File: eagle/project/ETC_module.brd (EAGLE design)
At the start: 100 x 80 mm, 102 parts, among them IC1 LM358, Q2 MOSFET-PCHANNELFQP27P06, U1 V_REG_317SMD

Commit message: v1.0 of ETC board complete
initial work on GS board underway too
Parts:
- added U$20: (no value), custom:NURLOGO
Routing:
- net GNDI: track 143.3 -> 96.0 mm
- net +5VCLEAN: track 316.0 -> 276.3 mm
- net N$41: track 17.1 -> 18.0 mm
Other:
- board size 100 x 80 mm -> 101.3 x 81.3 mm
- board text added: "ETC module V1.0"
- board text added: "www.github.com/francisconroy"

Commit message: finish version 1.0 of GS board
yay!
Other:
- board text added: "Franks Air Requirement Thingy"
- board text added: "github.com/francisconroy"
- board text removed: "www.github.com/francisconroy"
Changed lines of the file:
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@@
 <hole x="50.8" y="8.89" drill="3"/>
 <hole x="28.575" y="75.565" drill="3"/>
-<text x="45.72" y="77.47" size="1.27" layer="25">www.github.com/francisconroy</text>
-<text x="45.72" y="74.93" size="1.27" layer="25">ETC module V1.0</text>
+<text x="63.5" y="75.565" size="1.27" layer="25" rot="R180">github.com/francisconroy</text>
+<text x="38.1" y="54.61" size="1.27" layer="25" rot="R90">ETC module V1.0</text>
+<text x="60.325" y="0.635" size="1.27" layer="25">Franks Air Requirement Thingy</text>
 </plain>
 <attributes>

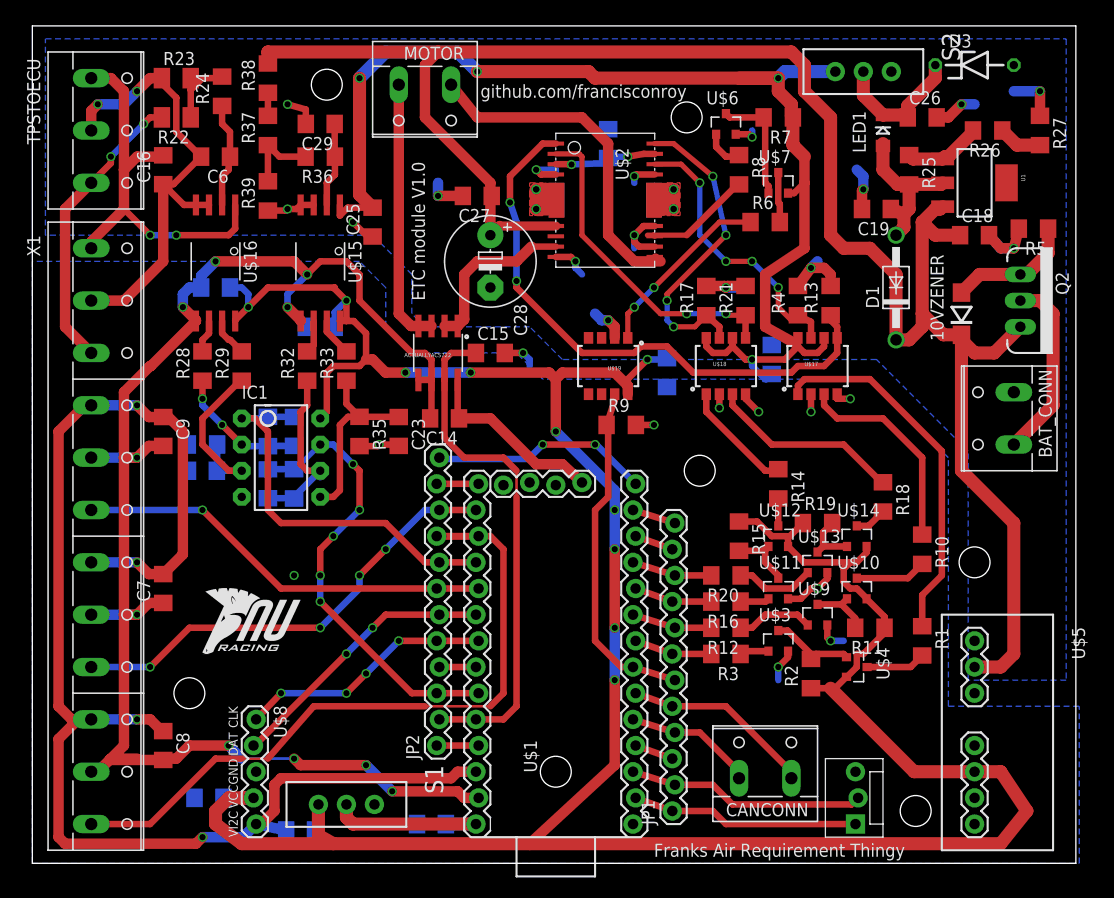
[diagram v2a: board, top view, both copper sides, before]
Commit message: Versions of the board which went to the fab house
Updating BOMS for component ordering
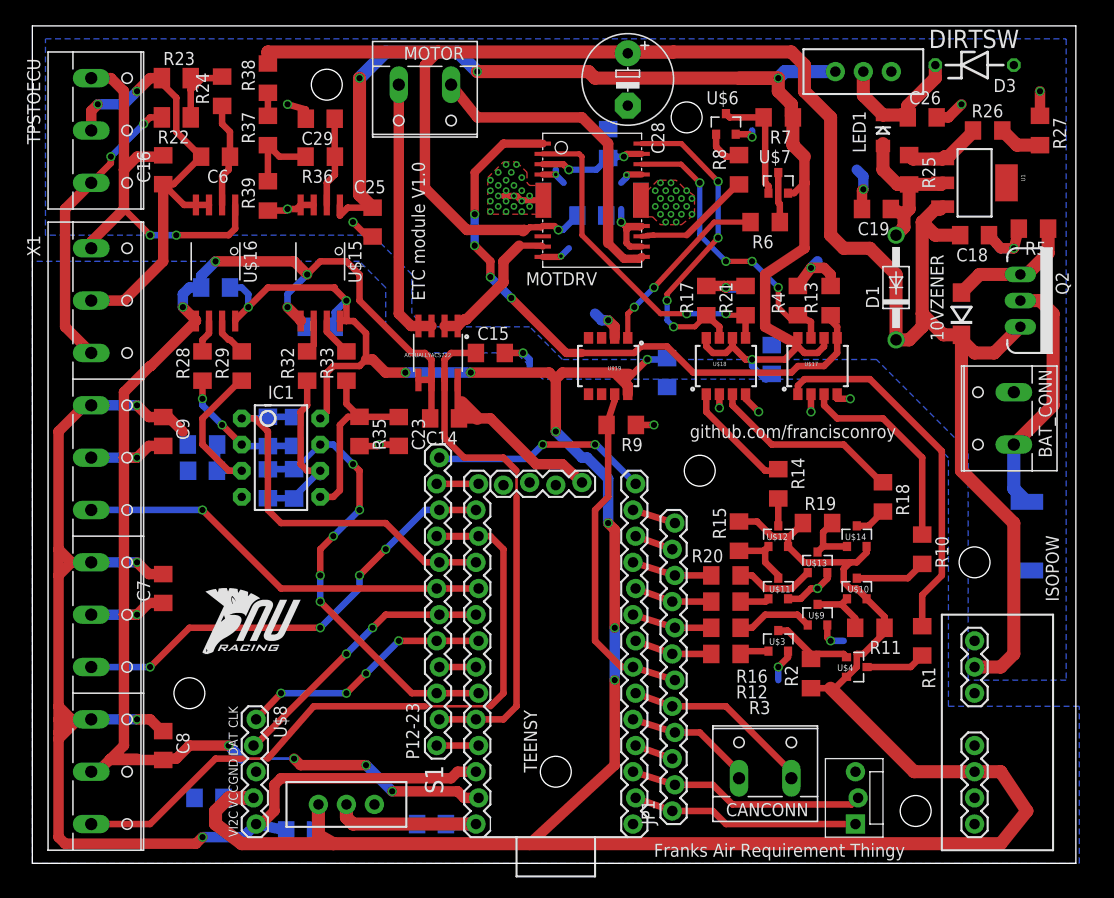
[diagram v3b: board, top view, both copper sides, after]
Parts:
- removed U$2: TB6559FG, custom:HSOP16-P-300-1.00
- added MOTDRV: TB6559FG, custom:HSOP16-P-300-1.00
- added TEENSY: TEENSY31DEV, custom:TEENSY31PAC
- U$1: value TEENSY31DEV -> LNBTVS; device custom:TEENSY31PAC -> custom:JEDECDO-214AB
- moved U$1 45.9 mm to (96.5, 31.8), flipped to the bottom, turned to 270 degrees
- moved C28 22.1 mm to (57.8, 76.1)
- moved C27 11.3 mm to (54.3, 62.9), flipped to the bottom
- moved C29 0.51 mm to (27.9, 72.3)
- renumbered JP2 to P12-23, S2 to DIRTSW, U$5 to ISOPOW
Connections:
- net +12V: now also MOTDRV.VCC; no longer U$2.VCC
- net +3V3: now also TEENSY.3.3V, TEENSY.3.3VV; no longer U$1.3.3V, U$1.3.3VV
- net 5VOUT: now also MOTDRV.VREF, MOTDRV.VREG; no longer U$2.VREF, U$2.VREG
- net AGND: now also TEENSY.AGND; no longer U$1.AGND
- net GND: now also TEENSY.GND, TEENSY.GND2; no longer U$1.GND, U$1.GND2
- net GNDI: now also MOTDRV.FIN, MOTDRV.FIN2, MOTDRV.P$20, MOTDRV.P$4, MOTDRV.P-GND, MOTDRV.RSA, MOTDRV.S-GND, MOTDRV.S-GND2, MOTDRV.S-GND3, U$1.A; no longer U$2.FIN, U$2.FIN2, U$2.P$20, U$2.P$4, U$2.P-GND, U$2.RSA, U$2.S-GND, U$2.S-GND2, U$2.S-GND3
- net N$13: now also U$1.K
- net N$19: now also MOTDRV.OUT2; no longer U$2.OUT2
- net N$2: now also TEENSY.VIN; no longer U$1.VIN
- net N$20: now also MOTDRV.OUT1; no longer U$2.OUT1
- net N$29: now also MOTDRV.IN2; no longer U$2.IN2
- net N$32: now also MOTDRV.ALERT; no longer U$2.ALERT
- net N$33: now also MOTDRV.SB; no longer U$2.SB
- net N$43: now also MOTDRV.IN1; no longer U$2.IN1
- net N$8: now also MOTDRV.PWM; no longer U$2.PWM
- net P0: now also TEENSY.0; no longer U$1.0
- net P1: now also TEENSY.1; no longer U$1.1
- net P10: now also TEENSY.10; no longer U$1.10
- net P11: now also TEENSY.11; no longer U$1.11
- net P12: now also TEENSY.12; no longer U$1.12
- net P13: now also TEENSY.13; no longer U$1.13
- net P14: now also TEENSY.14; no longer U$1.14
- net P15: now also TEENSY.15; no longer U$1.15
- net P16: now also TEENSY.16; no longer U$1.16
- net P17: now also TEENSY.17; no longer U$1.17
- net P18: now also TEENSY.18; no longer U$1.18
- net P19: now also TEENSY.19; no longer U$1.19
- net P2: now also TEENSY.2; no longer U$1.2
- net P20: now also TEENSY.20; no longer U$1.20
- net P21: now also TEENSY.21; no longer U$1.21
- net P22: now also TEENSY.22; no longer U$1.22
- net P23: now also TEENSY.23; no longer U$1.23
- net P3: now also TEENSY.3; no longer U$1.3
- net P4: now also TEENSY.4; no longer U$1.4
- net P5: now also TEENSY.5; no longer U$1.5
- net P6: now also TEENSY.6; no longer U$1.6
- net P7: now also TEENSY.7; no longer U$1.7
- net P8: now also TEENSY.8; no longer U$1.8
- net P9: now also TEENSY.9; no longer U$1.9
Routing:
- net GNDI: track 96.0 -> 65.0 mm, vias 20 -> 59
- net +12V: track 183.3 -> 191.2 mm, vias 0 -> 1
- net N$13: track 18.0 -> 24.1 mm
- net N$43: track 56.4 -> 61.3 mm, vias 2 -> 4
- net N$20: track 16.5 -> 14.0 mm
- net N$19: track 33.6 -> 31.4 mm
- net 5VOUT: track 9.89 -> 11.7 mm
- net N$33: track 31.6 -> 32.8 mm
- net N$8: track 27.4 -> 28.7 mm
- net N$29: track 30.6 -> 31.7 mm
- net N$56: track 0.00 -> 1.02 mm
- net N$32: track 11.1 -> 12.1 mm
- net +3V3: track 154.6 -> 153.9 mm
- net N$48: track 8.20 -> 8.70 mm
- net +5VCLEAN: track 276.3 -> 276.6 mm, vias 10 -> 9
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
